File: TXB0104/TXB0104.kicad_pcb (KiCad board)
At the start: 2 copper layers, 13 x 15.5 mm, 8 parts, among them J1 Conn_01x06, J2 Conn_01x06, U1 TXB0104D

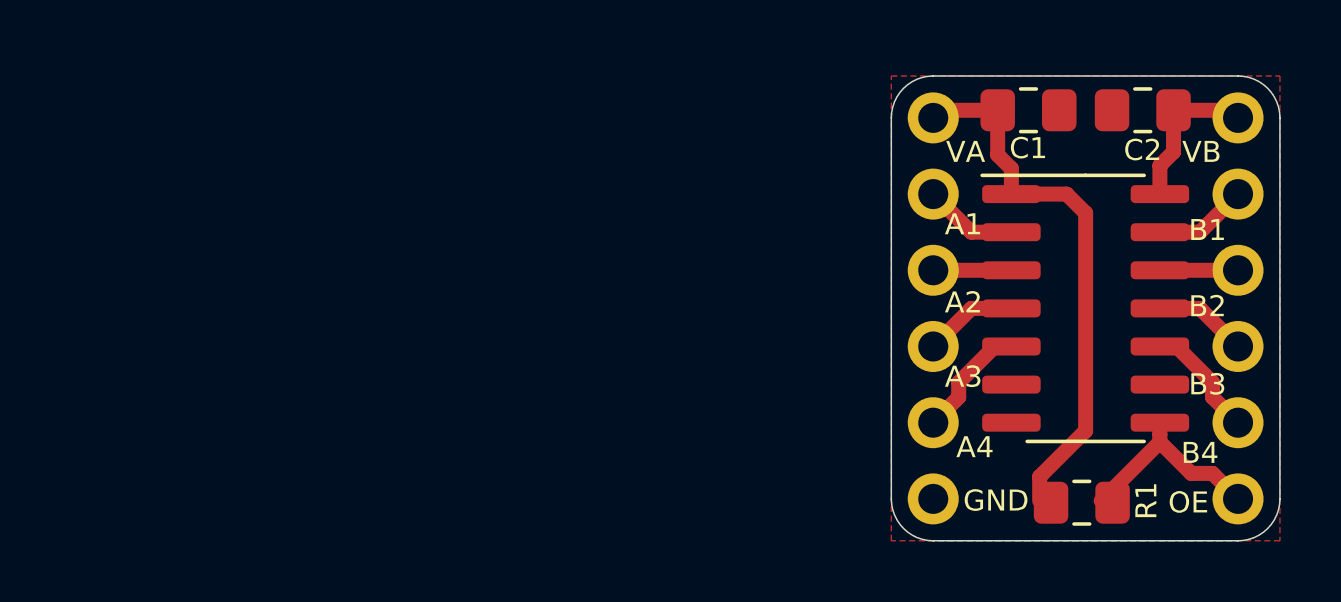
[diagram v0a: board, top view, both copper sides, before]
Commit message: SOIC8 Changed to TSSOP8
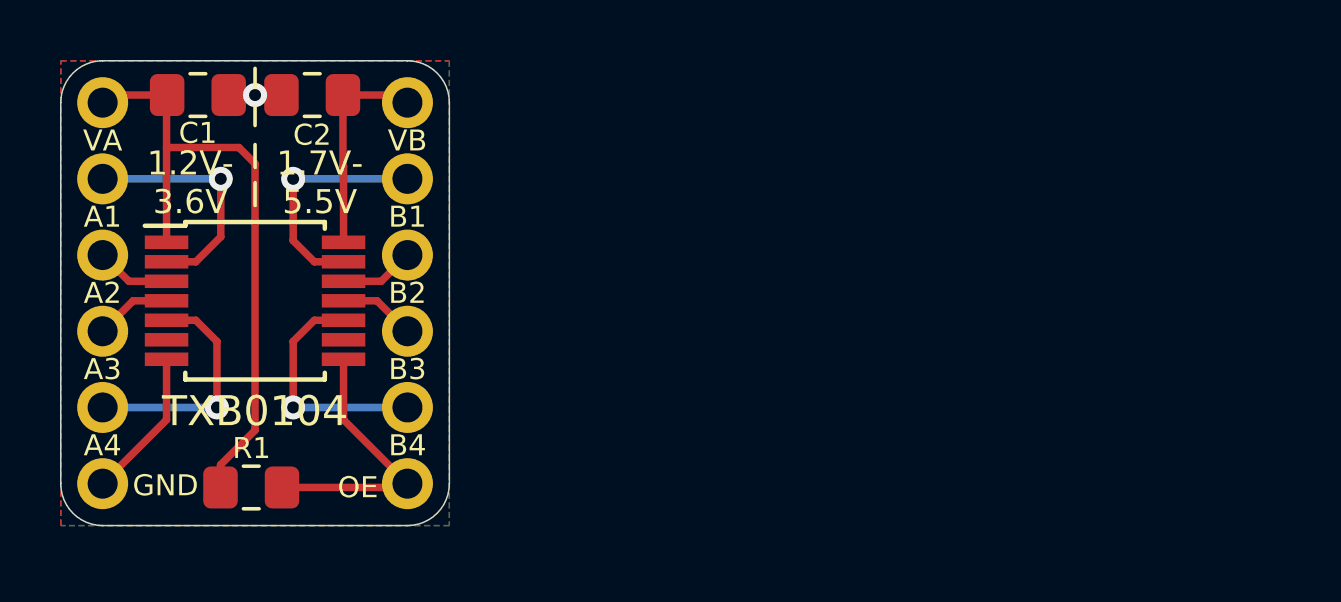
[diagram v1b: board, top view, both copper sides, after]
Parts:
- removed U1: TXB0104D, Package_SO:SOIC-14_3.9x8.7mm_P1.27mm
- added TXB0104: TXB0104PW, Package_SO:TSSOP-14_4.4x5mm_P0.65mm, F.Cu at (117.1, 105.2)
- moved C1 27.7 mm to (115.2, 98.3)
- moved C2 27.7 mm to (119.0, 98.3)
- moved G*** 27.7 mm to (117.1, 102.7)
- moved G*** 27.7 mm to (117.1, 99.4)
- moved J2 27.7 mm to (122.2, 98.6)
- moved J1 27.7 mm to (112.0, 98.6)
- moved R1 27.7 mm to (117.0, 111.4)
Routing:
- net /GND: track 0.00 -> 5.03 mm, vias 0 -> 1
- net /A1: track 3.13 -> 8.02 mm, vias 0 -> 1
- net /B1: track 3.13 -> 7.84 mm, vias 0 -> 1
- net /B4: track 3.94 -> 7.98 mm, vias 0 -> 1
- net /A4: track 3.94 -> 7.98 mm, vias 0 -> 1
- net /VLOW: track 18.2 -> 21.6 mm
- net /OE: track 7.16 -> 9.26 mm
- net /VHI: track 5.24 -> 7.17 mm
- net /B3: track 3.13 -> 2.55 mm
- net /A3: track 3.13 -> 2.55 mm
- added copper zone on B.Cu, net /GND
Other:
- board text added: "1.2V- 3.6V"
- board text added: "1.7V- 5.5V"
- board text added: "Bi-Directional Level Shifter VA:1.2-3.6 VB:1.7-5.5"
- board text removed: "Bi-Directional Level Shifter LV:1.2-3.6 HV:1.7-5.5"

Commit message: Silkscreen Updated
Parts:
- R1: value R_US -> 10k
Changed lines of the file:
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@@
   (general
     (thickness 1.6)
-    (drawings 29)
-    (tracks 50)
+    (drawings 33)
+    (tracks 51)
     (zones 0)
     (modules 8)
@@
   (layers
     (0 F.Cu signal)
-    (31 B.Cu signal hide)
+    (31 B.Cu signal)
     (32 B.Adhes user hide)
     (33 F.Adhes user hide)
@@
       (effects (font (size 0.7 0.7) (thickness 0.13)))
     )
-    (fp_text value R_US (at 0 1.65) (layer F.Fab)
+    (fp_text value 10k (at 0 1.65) (layer F.Fab)
       (effects (font (size 1 1) (thickness 0.15)))
     )
@@
     )
   )
+  (dimension 12.7 (width 0.15) (layer F.SilkS)
+    (gr_text "12.700 mm" (at 126.649 104.902 270) (layer F.SilkS)
+      (effects (font (size 1 1) (thickness 0.15)) hide)
+    )
+    (feature1 (pts (xy 122.174 111.252) (xy 125.935421 111.252)))
+    (feature2 (pts (xy 122.174 98.552) (xy 125.935421 98.552)))
+    (crossbar (pts (xy 125.349 98.552) (xy 125.349 111.252)))
+    (arrow1a (pts (xy 125.349 111.252) (xy 124.762579 110.125496)))
+    (arrow1b (pts (xy 125.349 111.252) (xy 125.935421 110.125496)))
+    (arrow2a (pts (xy 125.349 98.552) (xy 124.762579 99.678504)))
+    (arrow2b (pts (xy 125.349 98.552) (xy 125.935421 99.678504)))
+  )
+  (dimension 15.494 (width 0.15) (layer F.SilkS)
+    (gr_text "15.494 mm" (at 129.443 104.902 270) (layer F.SilkS)
+      (effects (font (size 1 1) (thickness 0.15)) hide)
+    )
+    (feature1 (pts (xy 123.571 112.649) (xy 128.729421 112.649)))
+    (feature2 (pts (xy 123.571 97.155) (xy 128.729421 97.155)))
+    (crossbar (pts (xy 128.143 97.155) (xy 128.143 112.649)))
+    (arrow1a (pts (xy 128.143 112.649) (xy 127.556579 111.522496)))
+    (arrow1b (pts (xy 128.143 112.649) (xy 128.729421 111.522496)))
+    (arrow2a (pts (xy 128.143 97.155) (xy 127.556579 98.281504)))
+    (arrow2b (pts (xy 128.143 97.155) (xy 128.729421 98.281504)))
+  )
+  (dimension 10.16 (width 0.15) (layer F.SilkS)
+    (gr_text "10.160 mm" (at 117.094 94.331) (layer F.SilkS)
+      (effects (font (size 1 1) (thickness 0.15)) hide)
+    )
+    (feature1 (pts (xy 122.174 98.552) (xy 122.174 95.044579)))
+    (feature2 (pts (xy 112.014 98.552) (xy 112.014 95.044579)))
+    (crossbar (pts (xy 112.014 95.631) (xy 122.174 95.631)))
+    (arrow1a (pts (xy 122.174 95.631) (xy 121.047496 96.217421)))
+    (arrow1b (pts (xy 122.174 95.631) (xy 121.047496 95.044579)))
+    (arrow2a (pts (xy 112.014 95.631) (xy 113.140504 96.217421)))
+    (arrow2b (pts (xy 112.014 95.631) (xy 113.140504 95.044579)))
+  )
+  (dimension 12.954 (width 0.15) (layer F.SilkS)
+    (gr_text "12.954 mm" (at 117.094 91.791) (layer F.SilkS)
+      (effects (font (size 1 1) (thickness 0.15)) hide)
+    )
+    (feature1 (pts (xy 123.571 97.155) (xy 123.571 92.504579)))
+    (feature2 (pts (xy 110.617 97.155) (xy 110.617 92.504579)))
+    (crossbar (pts (xy 110.617 93.091) (xy 123.571 93.091)))
+    (arrow1a (pts (xy 123.571 93.091) (xy 122.444496 93.677421)))
+    (arrow1b (pts (xy 123.571 93.091) (xy 122.444496 92.504579)))
+    (arrow2a (pts (xy 110.617 93.091) (xy 111.743504 93.677421)))
+    (arrow2b (pts (xy 110.617 93.091) (xy 111.743504 92.504579)))
+  )
   (gr_text "1.7V-\n5.5V" (at 119.253 101.219) (layer F.SilkS)
     (effects (font (size 0.8 0.8) (thickness 0.13)))
@@
   (segment (start 120.044 105.806) (end 119.069 105.806) (width 0.25) (layer F.Cu) (net 8))
   (segment (start 119.069 105.806) (end 118.364 106.511) (width 0.25) (layer F.Cu) (net 8))
-  (segment (start 118.364 108.712) (end 122.174 108.712) (width 0.25) (layer B.Cu) (net 8))
+  (segment (start 118.364 108.712) (end 118.872 108.712) (width 0.25) (layer B.Cu) (net 8))
+  (segment (start 118.872 108.712) (end 122.174 108.712) (width 0.25) (layer B.Cu) (net 8))
   (segment (start 121.158 105.156) (end 122.174 106.172) (width 0.25) (layer F.Cu) (net 9))
   (segment (start 120.044 105.156) (end 121.158 105.156) (width 0.25) (layer F.Cu) (net 9))

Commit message: Silkscreen Edits
Dimensions moved to Drawings Layer
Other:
- rule pad_to_mask_clearance: 0.051 -> 0
- rule solder_mask_min_width: 0.25 -> 0.1
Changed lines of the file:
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@@
     (pad_size 1.7 1.7)
     (pad_drill 1)
-    (pad_to_mask_clearance 0.051)
-    (solder_mask_min_width 0.25)
+    (pad_to_mask_clearance 0)
+    (solder_mask_min_width 0.1)
     (aux_axis_origin 0 0)
     (visible_elements 7FFFFFFF)
     (pcbplotparams
-      (layerselection 0x010fc_ffffffff)
+      (layerselection 0x010f0_ffffffff)
       (usegerberextensions false)
       (usegerberattributes false)
@@
       (viasonmask false)
       (mode 1)
-      (useauxorigin false)
+      (useauxorigin true)
       (hpglpennumber 1)
       (hpglpenspeed 20)
@@
       (psa4output false)
       (plotreference true)
-      (plotvalue true)
+      (plotvalue false)
       (plotinvisibletext false)
       (padsonsilk false)
@@
       (outputformat 1)
       (mirror false)
-      (drillshape 1)
+      (drillshape 0)
       (scaleselection 1)
-      (outputdirectory ""))
+      (outputdirectory "../../Gerbers/TXB0104/"))
   )
   (net 0 "")
@@
     )
   )
-  (dimension 12.7 (width 0.15) (layer F.SilkS)
-    (gr_text "12.700 mm" (at 126.649 104.902 270) (layer F.SilkS)
+  (dimension 12.7 (width 0.15) (layer Dwgs.User)
+    (gr_text "12.700 mm" (at 126.649 104.902 270) (layer Dwgs.User)
       (effects (font (size 1 1) (thickness 0.15)) hide)
     )
@@
     (arrow2b (pts (xy 125.349 98.552) (xy 125.935421 99.678504)))
   )
-  (dimension 15.494 (width 0.15) (layer F.SilkS)
-    (gr_text "15.494 mm" (at 129.443 104.902 270) (layer F.SilkS)
+  (dimension 15.494 (width 0.15) (layer Dwgs.User)
+    (gr_text "15.494 mm" (at 129.443 104.902 270) (layer Dwgs.User)
       (effects (font (size 1 1) (thickness 0.15)) hide)
     )
@@
     (arrow2b (pts (xy 128.143 97.155) (xy 128.729421 98.281504)))
   )
-  (dimension 10.16 (width 0.15) (layer F.SilkS)
-    (gr_text "10.160 mm" (at 117.094 94.331) (layer F.SilkS)
+  (dimension 10.16 (width 0.15) (layer Dwgs.User)
+    (gr_text "10.160 mm" (at 117.094 94.331) (layer Dwgs.User)
       (effects (font (size 1 1) (thickness 0.15)) hide)
     )
@@
     (arrow2b (pts (xy 112.014 95.631) (xy 113.140504 95.044579)))
   )
-  (dimension 12.954 (width 0.15) (layer F.SilkS)
-    (gr_text "12.954 mm" (at 117.094 91.791) (layer F.SilkS)
+  (dimension 12.954 (width 0.15) (layer Dwgs.User)
+    (gr_text "12.954 mm" (at 117.094 91.791) (layer Dwgs.User)
       (effects (font (size 1 1) (thickness 0.15)) hide)
     )

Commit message: Part Numbers Added
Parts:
- moved J2 82.1 mm to (71.4, 34.0)
- moved C1 82.1 mm to (64.4, 33.8)
- moved C2 82.1 mm to (68.2, 33.8)
- moved G*** 82.1 mm to (66.3, 34.9)
- moved J1 82.1 mm to (61.2, 34.0)
- moved R1 82.1 mm to (66.2, 46.9)
- moved TXB0104 82.1 mm to (66.3, 40.6)
- moved G*** 82.1 mm to (66.3, 38.2)
